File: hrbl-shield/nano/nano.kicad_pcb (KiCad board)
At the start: 2 copper layers, 79.8 x 140.1 mm, 61 parts, among them P1 Digital, P2 Analog, P3 CONN_01X01, P4 CONN_01X01, P5 CONN_01X01, P6 CONN_01X01, U1 SFH6206-3T, U10 SFH6206-3T, U11 SFH6206-3T, U12 SFH6206-3T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

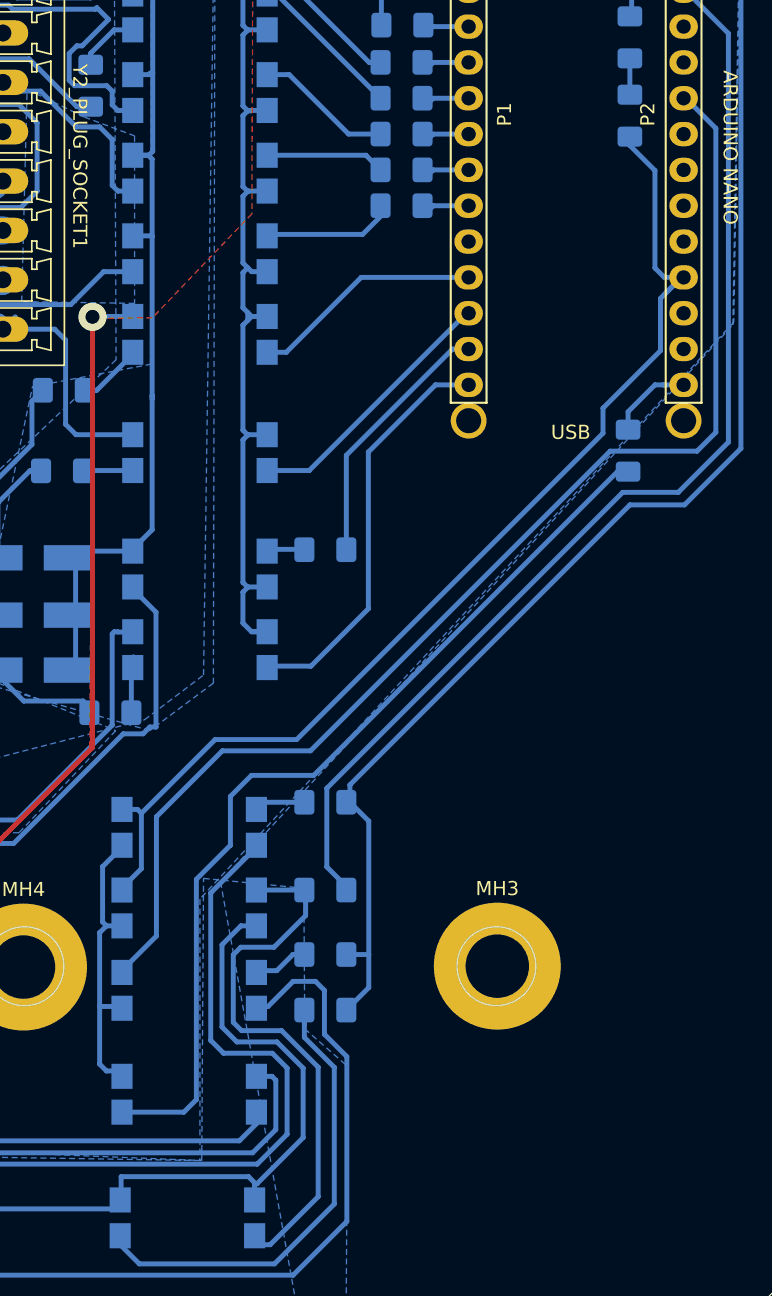
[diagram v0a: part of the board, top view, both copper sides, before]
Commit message: Hrbl with abort function (needs patch cable)
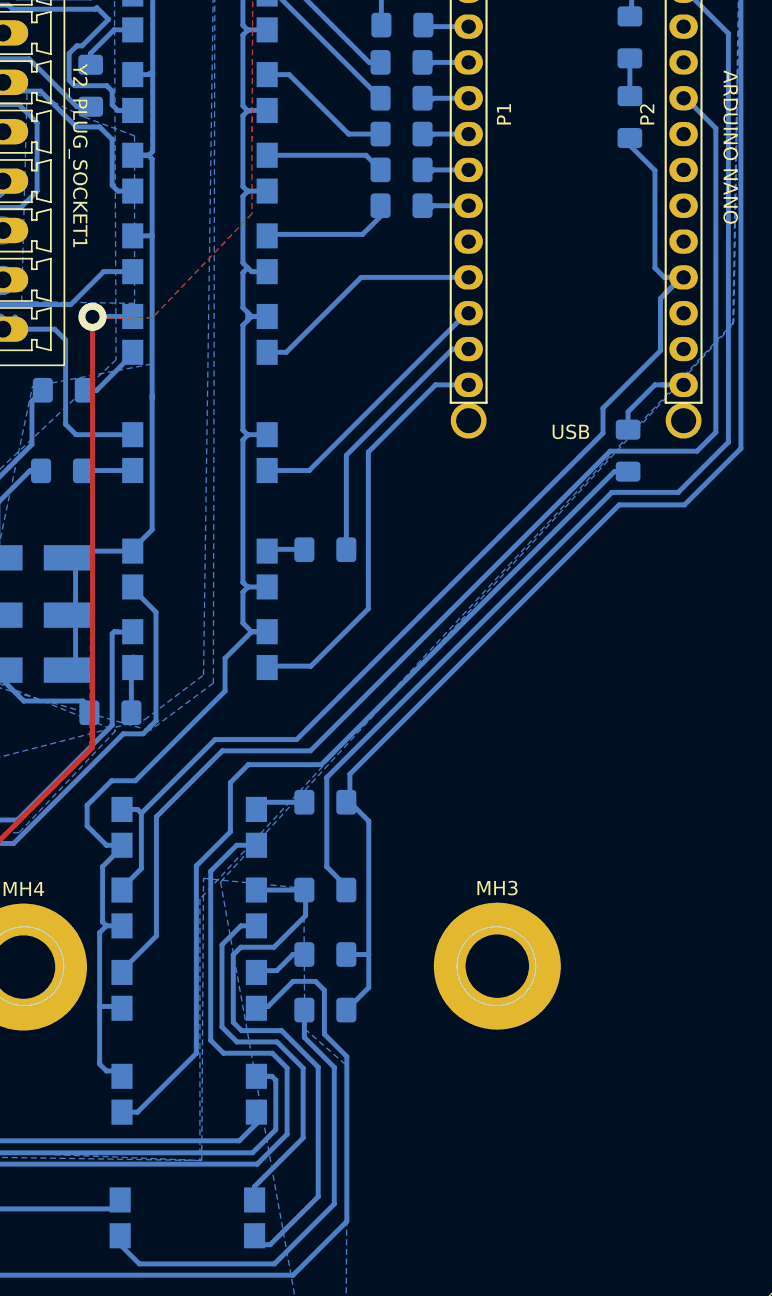
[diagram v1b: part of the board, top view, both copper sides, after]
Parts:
- removed R22: 220, Resistor_SMD:R_1206_3216Metric_Pad1.42x1.75mm_HandSolder
- added D1: LED, LED_SMD:LED_1206_3216Metric_Pad1.42x1.75mm_HandSolder, B.Cu at (150.9, 87.8)
- R16, R17, R18, R19, R20: value 0 RES -> 0
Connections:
- U1 pad 3: GNDS -> GND
- U2 pad 2: GNDS -> GND
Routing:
- net GND: track 122.4 -> 171.5 mm
- net GNDS: track 306.8 -> 268.8 mm
- net Net-(R10-Pad1): track 66.4 -> 65.0 mm
- net ALARM_IN: track 192.7 -> 193.5 mm
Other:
- board text added: "-|<-"
- board text added: "Cut and patch grounds"
- board text removed: "->|-"
- board text removed: "CUT AND MOVE"
- board text removed: "CUT FREE AND LINK TO 5V"

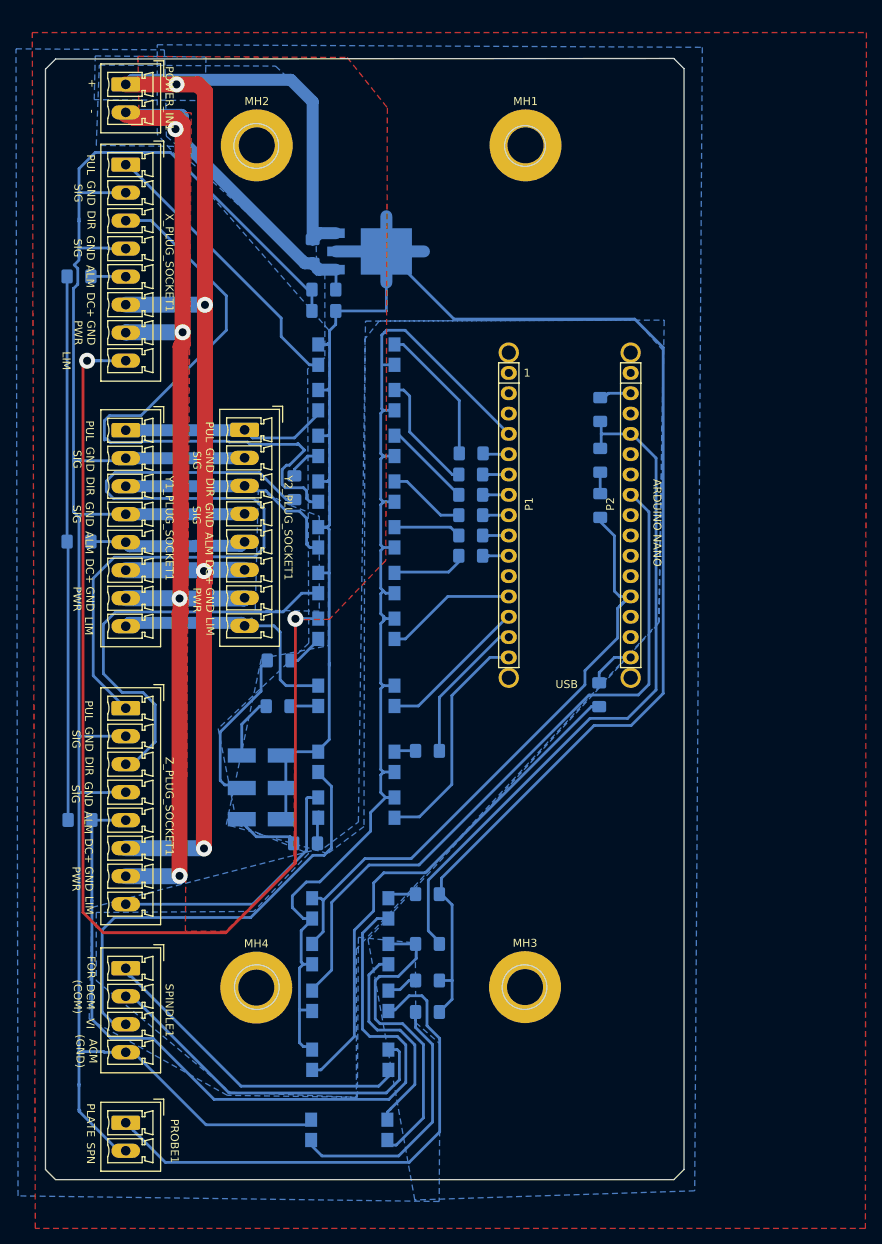
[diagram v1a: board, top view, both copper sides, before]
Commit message: Removed the need for patch cable
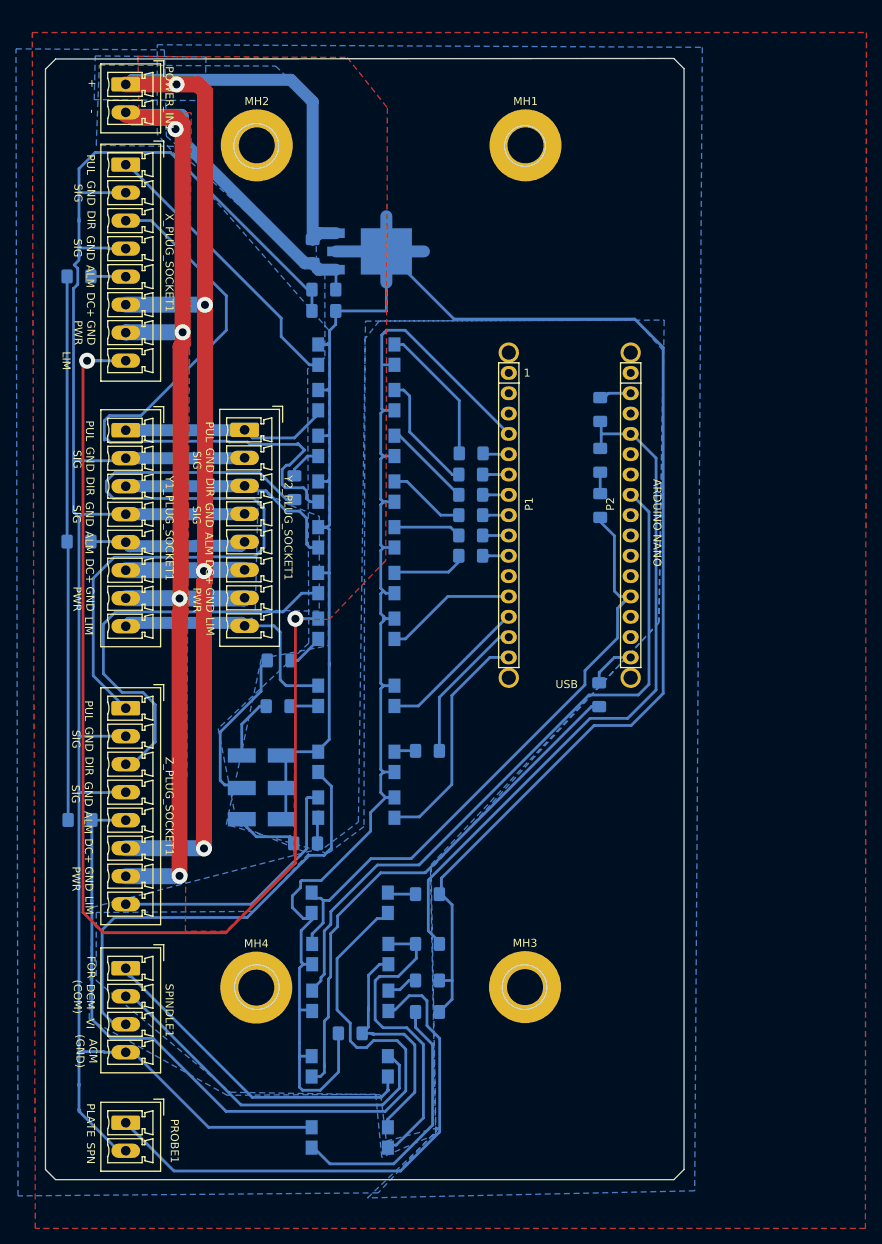
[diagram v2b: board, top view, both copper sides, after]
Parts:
- added R22: 0, Resistor_SMD:R_1206_3216Metric_Pad1.42x1.75mm_HandSolder, B.Cu at (119.6, 153.8)
- moved U1 0.95 mm to (119.6, 166.8)
- moved U13 0.83 mm to (119.6, 157.9)
- moved U3 0.70 mm to (119.6, 137.5)
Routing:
- net GND: track 171.5 -> 191.4 mm
- net ALARM_IN: track 193.5 -> 199.6 mm
- net /FOR: track 41.2 -> 42.4 mm
- net GNDS: track 268.8 -> 267.7 mm
- net Net-(R12-Pad1): track 32.1 -> 33.2 mm
- net /PROBE_PLATE: track 65.7 -> 66.6 mm
- net Net-(R10-Pad1): track 65.0 -> 65.8 mm
- net PROBE: track 87.7 -> 87.1 mm
- net /DCM(COM): track 45.4 -> 46.0 mm

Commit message: trimmed
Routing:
- net ALARM_IN: track 199.6 -> 201.6 mm
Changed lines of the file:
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@@
     (thickness 1.6)
     (drawings 95)
-    (tracks 644)
+    (tracks 645)
     (zones 0)
     (modules 62)
@@
   (segment (start 107.274114 137.657) (end 113.383104 131.54801) (width 0.35) (layer B.Cu) (net 33))
   (segment (start 91.567 137.657) (end 107.274114 137.657) (width 0.35) (layer B.Cu) (net 33))
-  (segment (start 122.9995 139.446) (end 124.399 139.446) (width 0.35) (layer B.Cu) (net 40))
-  (segment (start 117.983 150.876) (end 117.983 144.4625) (width 0.35) (layer B.Cu) (net 40))
-  (segment (start 119.634 154.7495) (end 119.634 152.527) (width 0.35) (layer B.Cu) (net 40))
-  (segment (start 120.4595 155.575) (end 119.634 154.7495) (width 0.35) (layer B.Cu) (net 40))
-  (segment (start 121.668454 155.575) (end 120.4595 155.575) (width 0.35) (layer B.Cu) (net 40))
-  (segment (start 122.544932 154.698522) (end 121.668454 155.575) (width 0.35) (layer B.Cu) (net 40))
-  (segment (start 119.634 152.527) (end 117.983 150.876) (width 0.35) (layer B.Cu) (net 40))
-  (segment (start 125.488522 154.698522) (end 122.544932 154.698522) (width 0.35) (layer B.Cu) (net 40))
-  (segment (start 126.574012 155.784012) (end 125.488522 154.698522) (width 0.35) (layer B.Cu) (net 40))
-  (segment (start 89.750311 154.432) (end 94.996 154.432) (width 0.35) (layer B.Cu) (net 40))
+  (segment (start 123.7005 138.7475) (end 124.399 139.446) (width 0.35) (layer B.Cu) (net 40))
+  (segment (start 126.574012 160.99426) (end 126.574012 155.784012) (width 0.35) (layer B.Cu) (net 40))
+  (segment (start 124.017761 163.550511) (end 126.574012 160.99426) (width 0.35) (layer B.Cu) (net 40))
   (segment (start 94.996 154.432) (end 104.114511 163.550511) (width 0.35) (layer B.Cu) (net 40))
-  (segment (start 117.983 144.4625) (end 122.9995 139.446) (width 0.35) (layer B.Cu) (net 40))
   (segment (start 89.408 154.089689) (end 89.750311 154.432) (width 0.35) (layer B.Cu) (net 40))
+  (segment (start 89.750311 154.432) (end 94.996 154.432) (width 0.35) (layer B.Cu) (net 40))
   (segment (start 104.114511 163.550511) (end 124.017761 163.550511) (width 0.35) (layer B.Cu) (net 40))
-  (segment (start 124.017761 163.550511) (end 126.574012 160.99426) (width 0.35) (layer B.Cu) (net 40))
-  (segment (start 126.574012 160.99426) (end 126.574012 155.784012) (width 0.35) (layer B.Cu) (net 40))
+  (segment (start 126.574012 155.784012) (end 125.488522 154.698522) (width 0.35) (layer B.Cu) (net 40))
+  (segment (start 125.488522 154.698522) (end 122.544932 154.698522) (width 0.35) (layer B.Cu) (net 40))
+  (segment (start 122.544932 154.698522) (end 121.668454 155.575) (width 0.35) (layer B.Cu) (net 40))
+  (segment (start 117.983 150.876) (end 117.983 141.986) (width 0.35) (layer B.Cu) (net 40))
+  (segment (start 121.668454 155.575) (end 120.4595 155.575) (width 0.35) (layer B.Cu) (net 40))
+  (segment (start 120.4595 155.575) (end 119.634 154.7495) (width 0.35) (layer B.Cu) (net 40))
+  (segment (start 119.634 154.7495) (end 119.634 152.527) (width 0.35) (layer B.Cu) (net 40))
+  (segment (start 119.634 152.527) (end 117.983 150.876) (width 0.35) (layer B.Cu) (net 40))
+  (segment (start 117.983 141.986) (end 121.2215 138.7475) (width 0.35) (layer B.Cu) (net 40))
+  (segment (start 121.2215 138.7475) (end 123.7005 138.7475) (width 0.35) (layer B.Cu) (net 40))
   (segment (start 92.53771 165.94371) (end 91.567 164.973) (width 0.35) (layer B.Cu) (net 41))
   (segment (start 97.5995 171.0055) (end 92.53771 165.94371) (width 0.35) (layer B.Cu) (net 41))
@@
     (connect_pads (clearance 0.75))
     (min_thickness 0.35)
-    (fill (arc_segments 16) (thermal_gap 0.45) (thermal_bridge_width 0.4))
+    (fill yes (arc_segments 16) (thermal_gap 0.45) (thermal_bridge_width 0.4))
     (polygon
       (pts
@@
     (connect_pads (clearance 0.75))
     (min_thickness 0.35)
-    (fill (arc_segments 16) (thermal_gap 0.45) (thermal_bridge_width 0.5))
+    (fill yes (arc_segments 16) (thermal_gap 0.45) (thermal_bridge_width 0.5))
     (polygon
       (pts
@@
     (connect_pads (clearance 0.75))
     (min_thickness 0.35)
-    (fill (arc_segments 16) (thermal_gap 0.45) (thermal_bridge_width 0.5))
+    (fill yes (arc_segments 16) (thermal_gap 0.45) (thermal_bridge_width 0.5))
     (polygon
       (pts
@@
     (connect_pads (clearance 0.75))
     (min_thickness 0.35)
-    (fill (arc_segments 16) (thermal_gap 0.45) (thermal_bridge_width 0.5) (smoothing fillet) (radius 2))
+    (fill yes (arc_segments 16) (thermal_gap 0.45) (thermal_bridge_width 0.5) (smoothing fillet) (radius 2))
     (polygon
       (pts
@@
     (connect_pads (clearance 0.75))
     (min_thickness 0.35)
-    (fill (arc_segments 16) (thermal_gap 0.45) (thermal_bridge_width 0.5) (smoothing fillet) (radius 2))
+    (fill yes (arc_segments 16) (thermal_gap 0.45) (thermal_bridge_width 0.5) (smoothing fillet) (radius 2))
     (polygon
       (pts
@@
     (connect_pads (clearance 0.75))
     (min_thickness 0.35)
-    (fill (arc_segments 16) (thermal_gap 0.45) (thermal_bridge_width 0.5) (smoothing fillet) (radius 2))
+    (fill yes (arc_segments 16) (thermal_gap 0.45) (thermal_bridge_width 0.5) (smoothing fillet) (radius 2))
     (polygon
       (pts
@@
     (connect_pads (clearance 0.75))
     (min_thickness 0.35)
-    (fill (arc_segments 16) (thermal_gap 0.45) (thermal_bridge_width 0.5))
+    (fill yes (arc_segments 16) (thermal_gap 0.45) (thermal_bridge_width 0.5))
     (polygon
       (pts
@@
     (connect_pads (clearance 0.75))
     (min_thickness 0.35)
-    (fill (arc_segments 16) (thermal_gap 0.45) (thermal_bridge_width 0.45))
+    (fill yes (arc_segments 16) (thermal_gap 0.45) (thermal_bridge_width 0.45))
     (polygon
       (pts

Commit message: nano update to fix issues
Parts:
- added C4: 100nF, Capacitor_SMD:C_1206_3216Metric_Pad1.42x1.75mm_HandSolder, B.Cu at (96.1, 154.6)
- added C5: 10uF, Capacitor_SMD:C_1206_3216Metric_Pad1.42x1.75mm_HandSolder, B.Cu at (112.1, 56.0)
- added C6: 10uF, Capacitor_SMD:C_1206_3216Metric_Pad1.42x1.75mm_HandSolder, B.Cu at (148.4, 75.2)
- added R23: 1000, Resistor_SMD:R_1206_3216Metric_Pad1.42x1.75mm_HandSolder, B.Cu at (143.8, 98.9)
- added R24: 1000, Resistor_SMD:R_1206_3216Metric_Pad1.42x1.75mm_HandSolder, B.Cu at (143.8, 101.7)
- added R25: 1000, Resistor_SMD:R_1206_3216Metric_Pad1.42x1.75mm_HandSolder, B.Cu at (143.8, 104.5)
- added R26: 1000, Resistor_SMD:R_1206_3216Metric_Pad1.42x1.75mm_HandSolder, B.Cu at (151.6, 82.2)
- moved R21 2.22 mm to (148.7, 82.2)
- moved D1 0.97 mm to (150.1, 87.3), turned to 180 degrees
- moved C3 0.78 mm to (151.3, 75.2)
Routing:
- net +5V: track 87.3 -> 119.4 mm
- net 5V_ISO: track 247.2 -> 260.2 mm
- net /VI: track 56.4 -> 61.1 mm
- net GNDPWR: track 169.9 -> 174.5 mm
- net PROBE: track 87.1 -> 91.3 mm
- net LIM_Z: track 29.0 -> 32.8 mm
- net LIM_X: track 16.4 -> 19.4 mm
- net LIM_Y: track 18.9 -> 21.7 mm
- net +36V: track 186.0 -> 188.8 mm
- net GND: track 191.4 -> 193.7 mm
- net ABORT: track 79.5 -> 81.4 mm
- net Net-(D1-Pad2): track 2.58 -> 3.53 mm

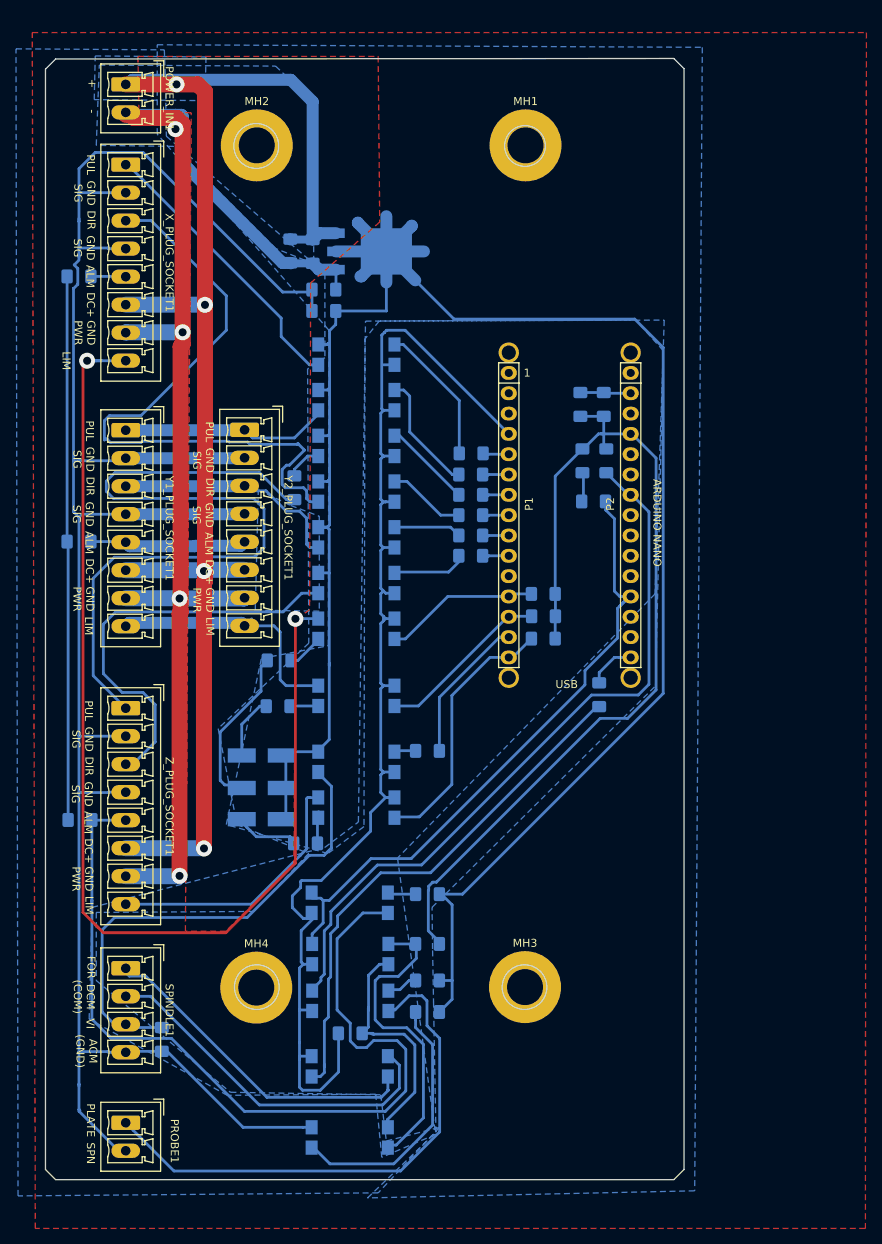
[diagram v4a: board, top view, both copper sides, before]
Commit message: Fixes to 8pin connector version. Can now be archived.
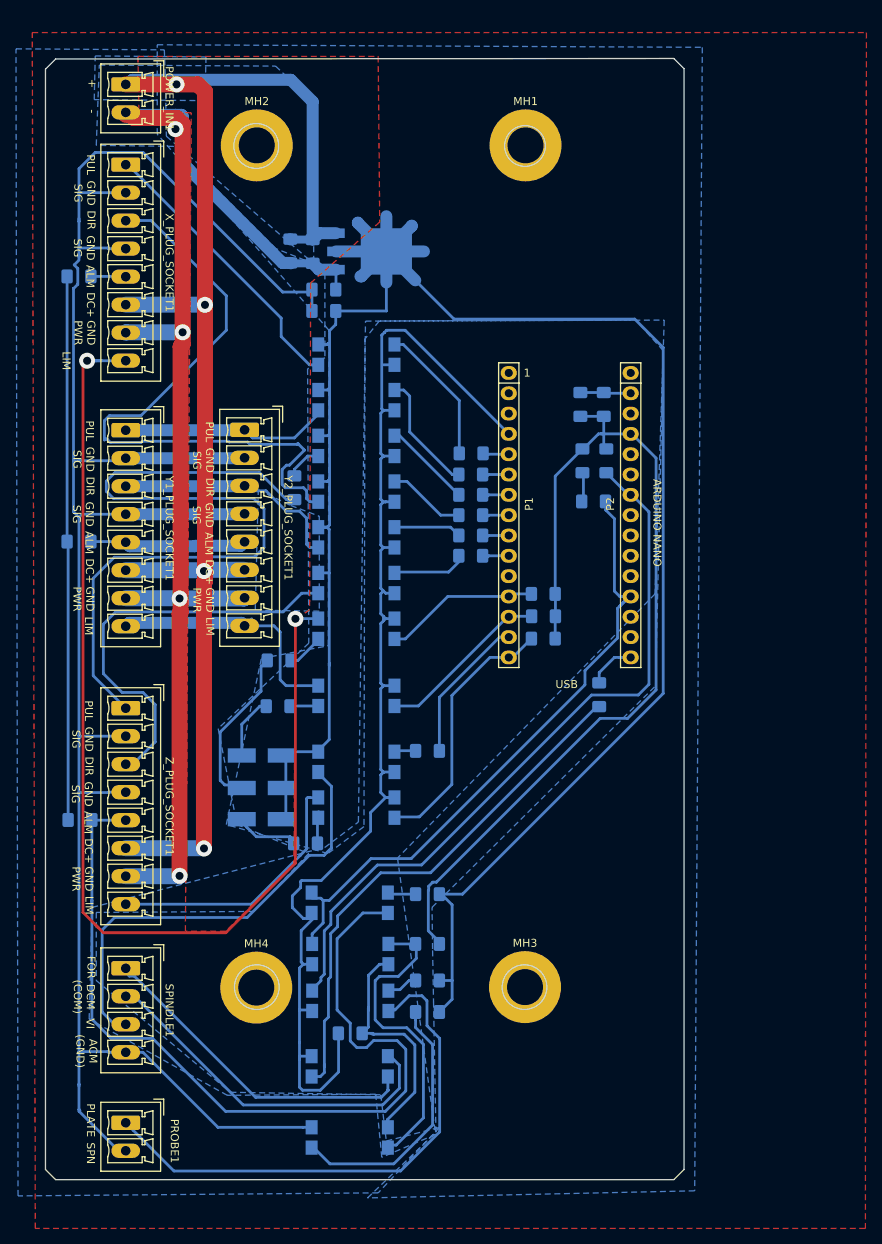
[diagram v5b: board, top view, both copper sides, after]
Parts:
- removed C4: 100nF, Capacitor_SMD:C_1206_3216Metric_Pad1.42x1.75mm_HandSolder
- removed P3, P4, P5, P6: CONN_01X01, Socket_Arduino_Nano:1pin_Nano
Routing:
- net /VI: track 61.1 -> 57.0 mm
